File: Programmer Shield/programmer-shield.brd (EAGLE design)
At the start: 80 x 73.7 mm, 26 parts, among them T1 2N3904, T2 2N3904, T3 2N3904, T4 2N3904, U1 SPARK_CORECORE, U2 RELAYSONGLE, U3 RELAYSONGLE, U4 RELAYSONGLE, U5 RELAYSONGLE

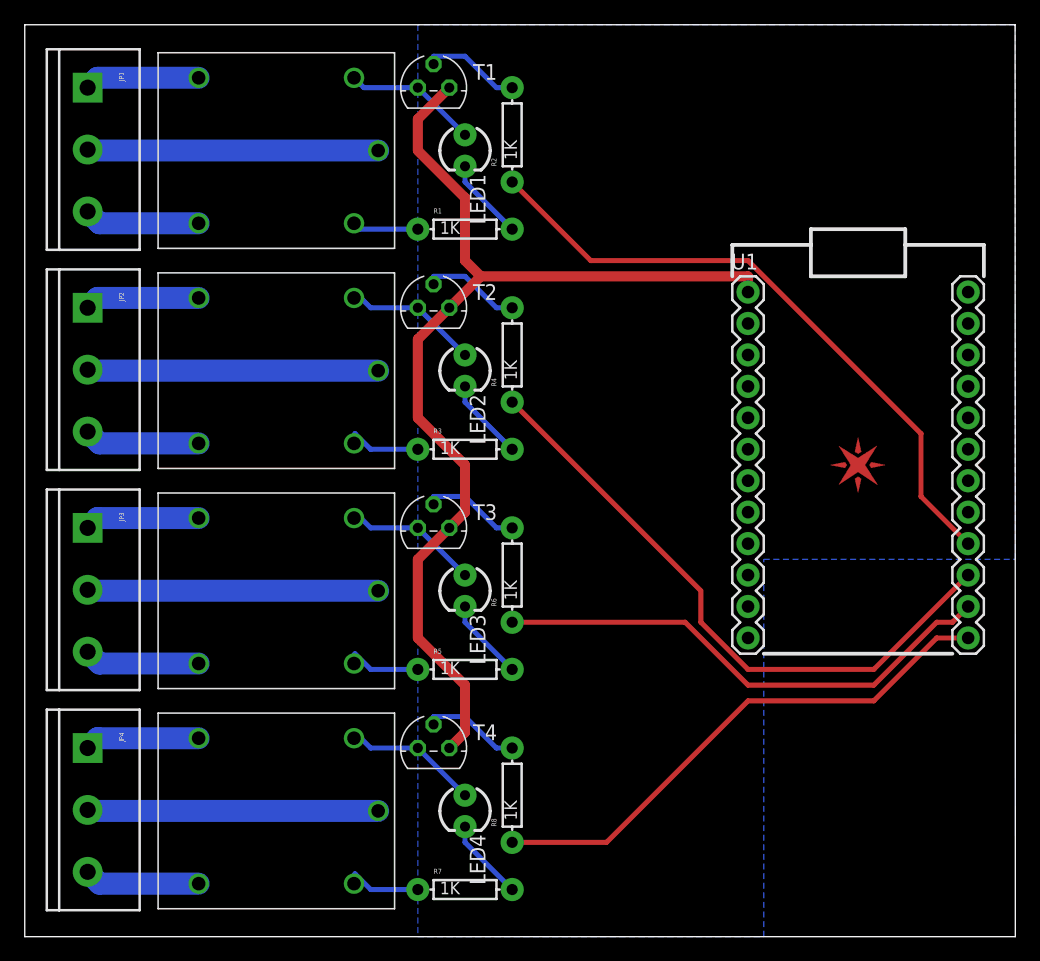
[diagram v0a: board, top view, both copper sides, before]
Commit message: Fixed programmer shield
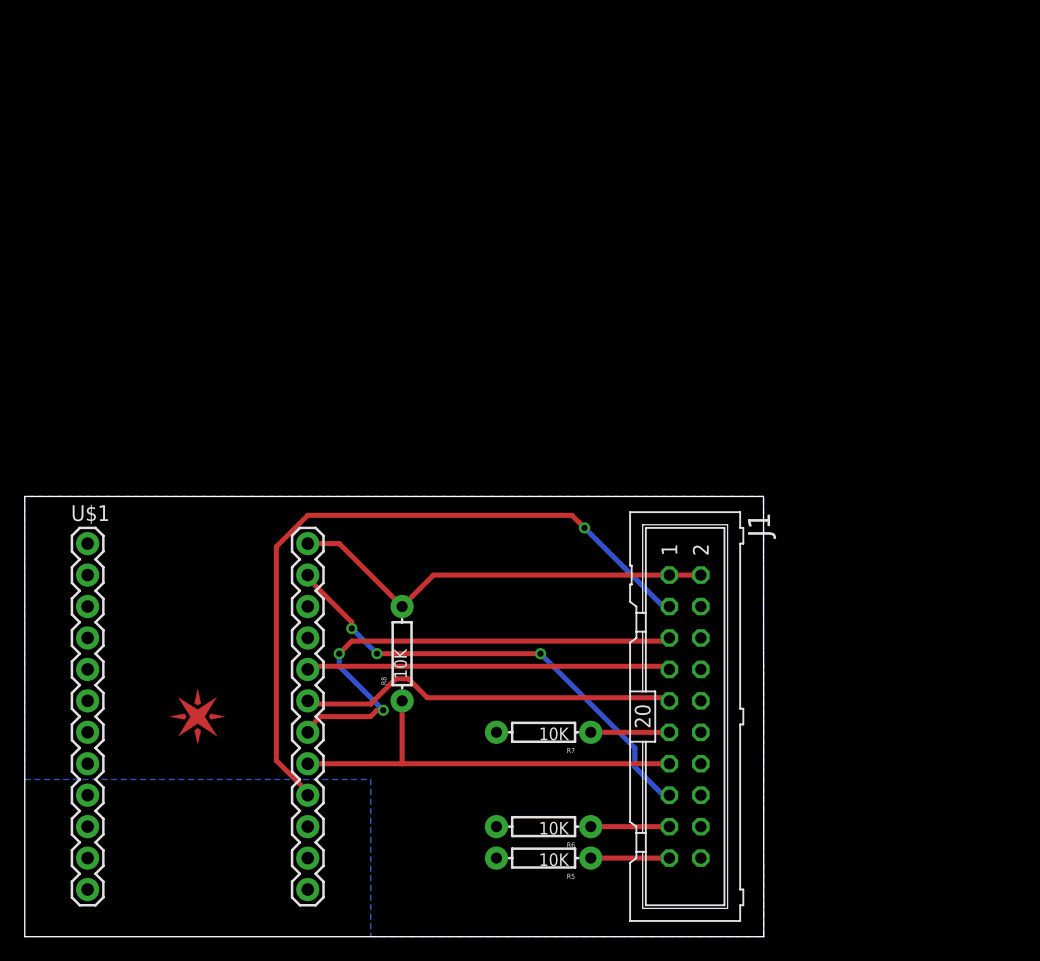
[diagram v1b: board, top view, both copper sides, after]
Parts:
- removed JP1, JP2, JP3, JP4: (no value), SparkFun-Connectors:SCREWTERMINAL-5MM-3
- removed LED1, LED2, LED3, LED4: (no value), SparkFun-LED:LED3MM
- removed R1, R2, R3, R4: 1K, SparkFun-Passives:AXIAL-0.3
- removed T1, T2, T3, T4: 2N3904, transistor:TO92
- removed U1: SPARK_CORECORE, Spark:SPARK_CORE
- removed U2, U3, U4, U5: RELAYSONGLE, Spark:SRD-5VDC-SL-C
- added J1: (no value), con-harting-ml:ML20
- added U$1: SPARK_CORECORE, Spark:SPARK_CORE
- R5, R6, R7, R8: value 1K -> 10K
- moved E$1 57.1 mm to (14.0, 17.8)
- moved R6 20.5 mm to (41.9, 8.89), turned to 180 degrees
- moved R5 16.5 mm to (41.9, 6.35), turned to 180 degrees
- moved R8 14.5 mm to (30.5, 22.9)
- moved R7 14.2 mm to (41.9, 16.5), turned to 180 degrees
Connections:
- removed net +5V: T1.1, T2.1, T3.1, T4.1, U1.1
- removed net MAIN1: JP1.2, U2.COMMON
- removed net MAIN2: JP2.2, U3.COMMON
- removed net MAIN3: JP3.2, U4.COMMON
- removed net MAIN4: JP4.2, U5.COMMON
- removed net N$1: LED1.A, T1.3, U2.COIL1
- removed net N$10: LED4.A, T4.3, U5.COIL1
- removed net N$11: R8.P$2, T4.2
- removed net N$12: LED4.K, R7.P$2
- removed net N$2: LED2.A, T2.3, U3.COIL1
- removed net N$3: R2.P$2, T1.2
- removed net N$4: LED1.K, R1.P$2
- removed net N$5: R4.P$2, T2.2
- removed net N$6: LED2.K, R3.P$2
- removed net N$7: LED3.A, T3.3, U4.COIL1
- removed net N$8: R6.P$2, T3.2
- removed net N$9: LED3.K, R5.P$2
- removed net NC1: JP1.3, U2.CLOSED
- removed net NC2: JP2.3, U3.CLOSED
- removed net NC3: JP3.3, U4.CLOSED
- removed net NC4: JP4.3, U5.CLOSED
- removed net NO1: JP1.1, U2.OPEN
- removed net NO2: JP2.1, U3.OPEN
- removed net NO3: JP3.1, U4.OPEN
- removed net NO4: JP4.1, U5.OPEN
- removed net RELAY1: R2.P$1, U1.16
- removed net RELAY2: R4.P$1, U1.15
- removed net RELAY3: R6.P$1, U1.14
- removed net RELAY4: R8.P$1, U1.13
- removed net VCC: U1.24
- new net !RST: J1.15, U$1.23
- new net +3V3: J1.1, J1.2, R8.P$2, U$1.24
- new net N$13: J1.19, R5.P$1
- new net N$14: J1.17, R6.P$1
- new net N$15: J1.11, R7.P$1
- new net RAW: U$1.1
- new net TCK: J1.9, U$1.19
- new net TDI: J1.5, U$1.18
- new net TDO: J1.13, R8.P$1, U$1.17
- new net TMS: J1.7, U$1.20
- new net TRST: J1.3, U$1.16
- net GND: now also J1.10, J1.12, J1.14, J1.16, J1.18, J1.20, J1.4, J1.6, J1.8, R5.P$2, R6.P$2, R7.P$2, U$1.2, U$1.21; no longer R1.P$1, R3.P$1, R5.P$1, R7.P$1, U1.2, U1.21, U2.COIL2, U3.COIL2, U4.COIL2, U5.COIL2
- net VDDA: now also U$1.22; no longer U1.22
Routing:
- net +5V: track 86.7 -> 0.00 mm
- net TRST: track 0.00 -> 57.2 mm, vias 0 -> 1
- net RELAY1: track 51.9 -> 0.00 mm
- net RELAY2: track 50.4 -> 0.00 mm
- net RELAY4: track 43.7 -> 0.00 mm
- net RELAY3: track 41.6 -> 0.00 mm
- net TDI: track 0.00 -> 40.2 mm, vias 0 -> 2
- net !RST: track 0.00 -> 38.1 mm, vias 0 -> 3
- net +3V3: track 0.00 -> 34.9 mm
- net TDO: track 0.00 -> 34.3 mm
- net TCK: track 0.00 -> 31.0 mm
- net TMS: track 0.00 -> 29.6 mm
- net GND: track 24.6 -> 0.00 mm
- net MAIN4: track 23.5 -> 0.00 mm
- net MAIN3: track 23.5 -> 0.00 mm
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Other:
- board size 80 x 73.7 mm -> 59.7 x 35.6 mm
- board text added: "2013-04-02"
- board text added: "Spark Programmer Shield"
- board text removed: "2013-04-15"
- board text removed: "Spark Relay Shield"
